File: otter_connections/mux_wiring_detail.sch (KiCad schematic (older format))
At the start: 21 parts

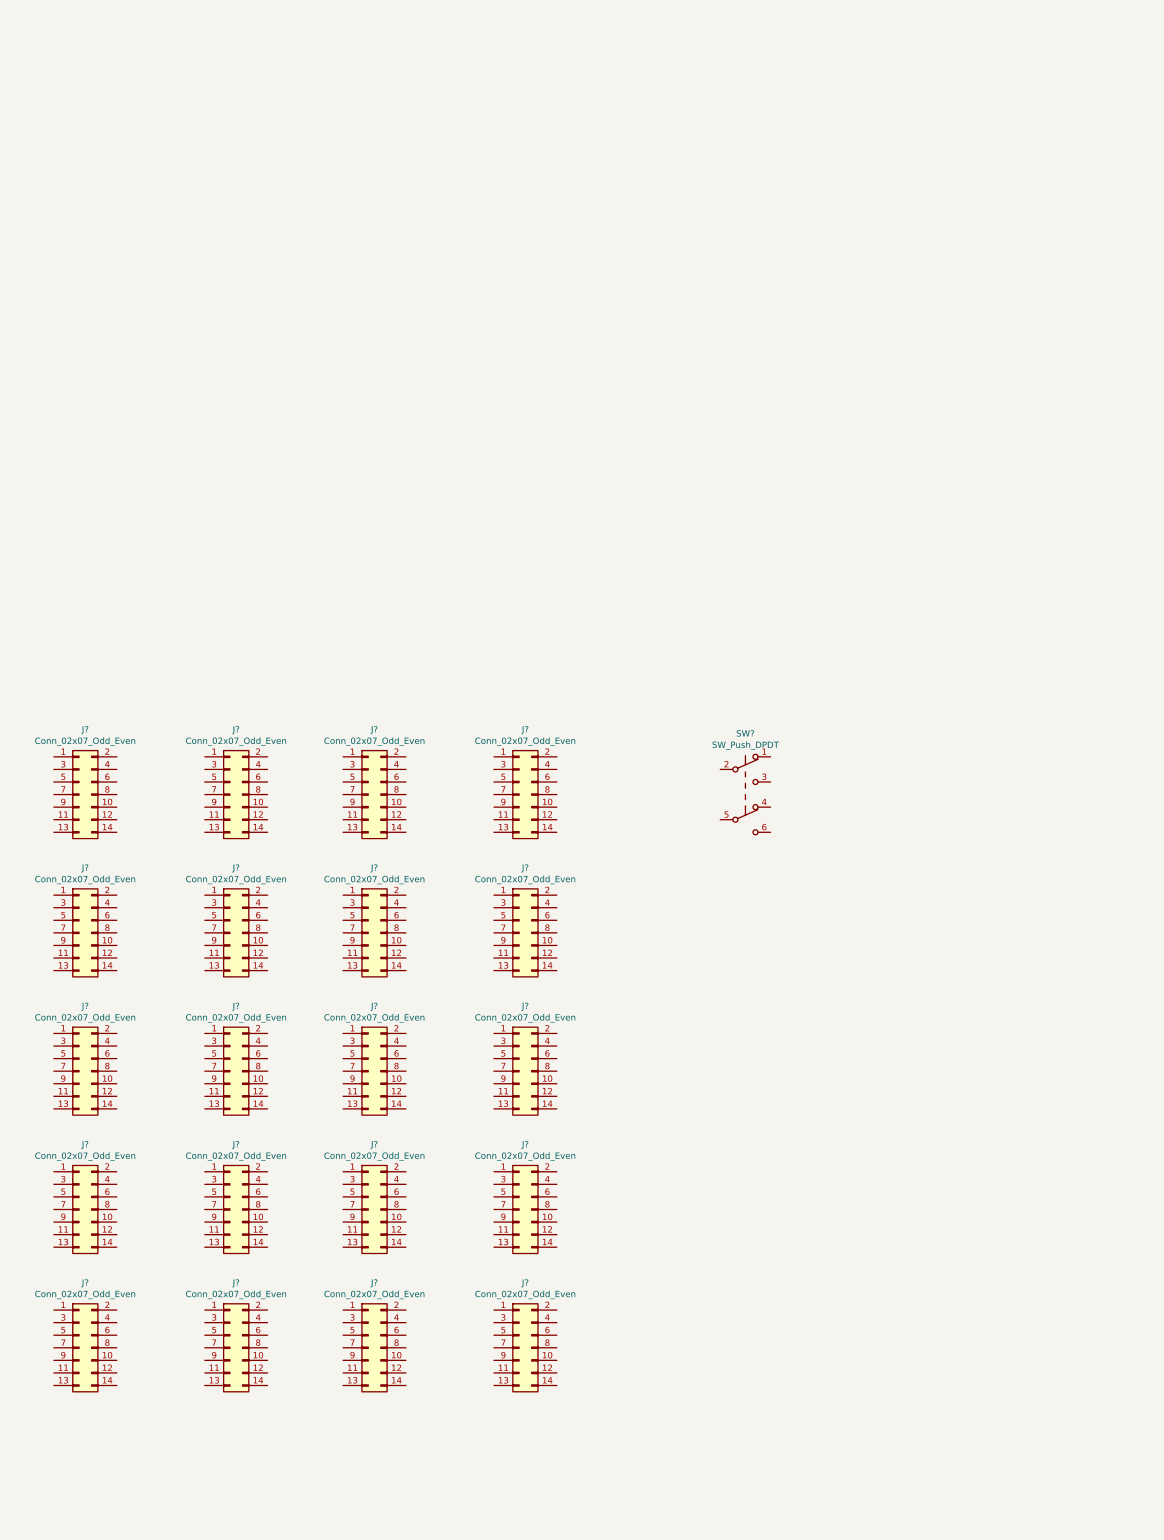
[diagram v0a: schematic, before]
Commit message: fix baseboard connector position
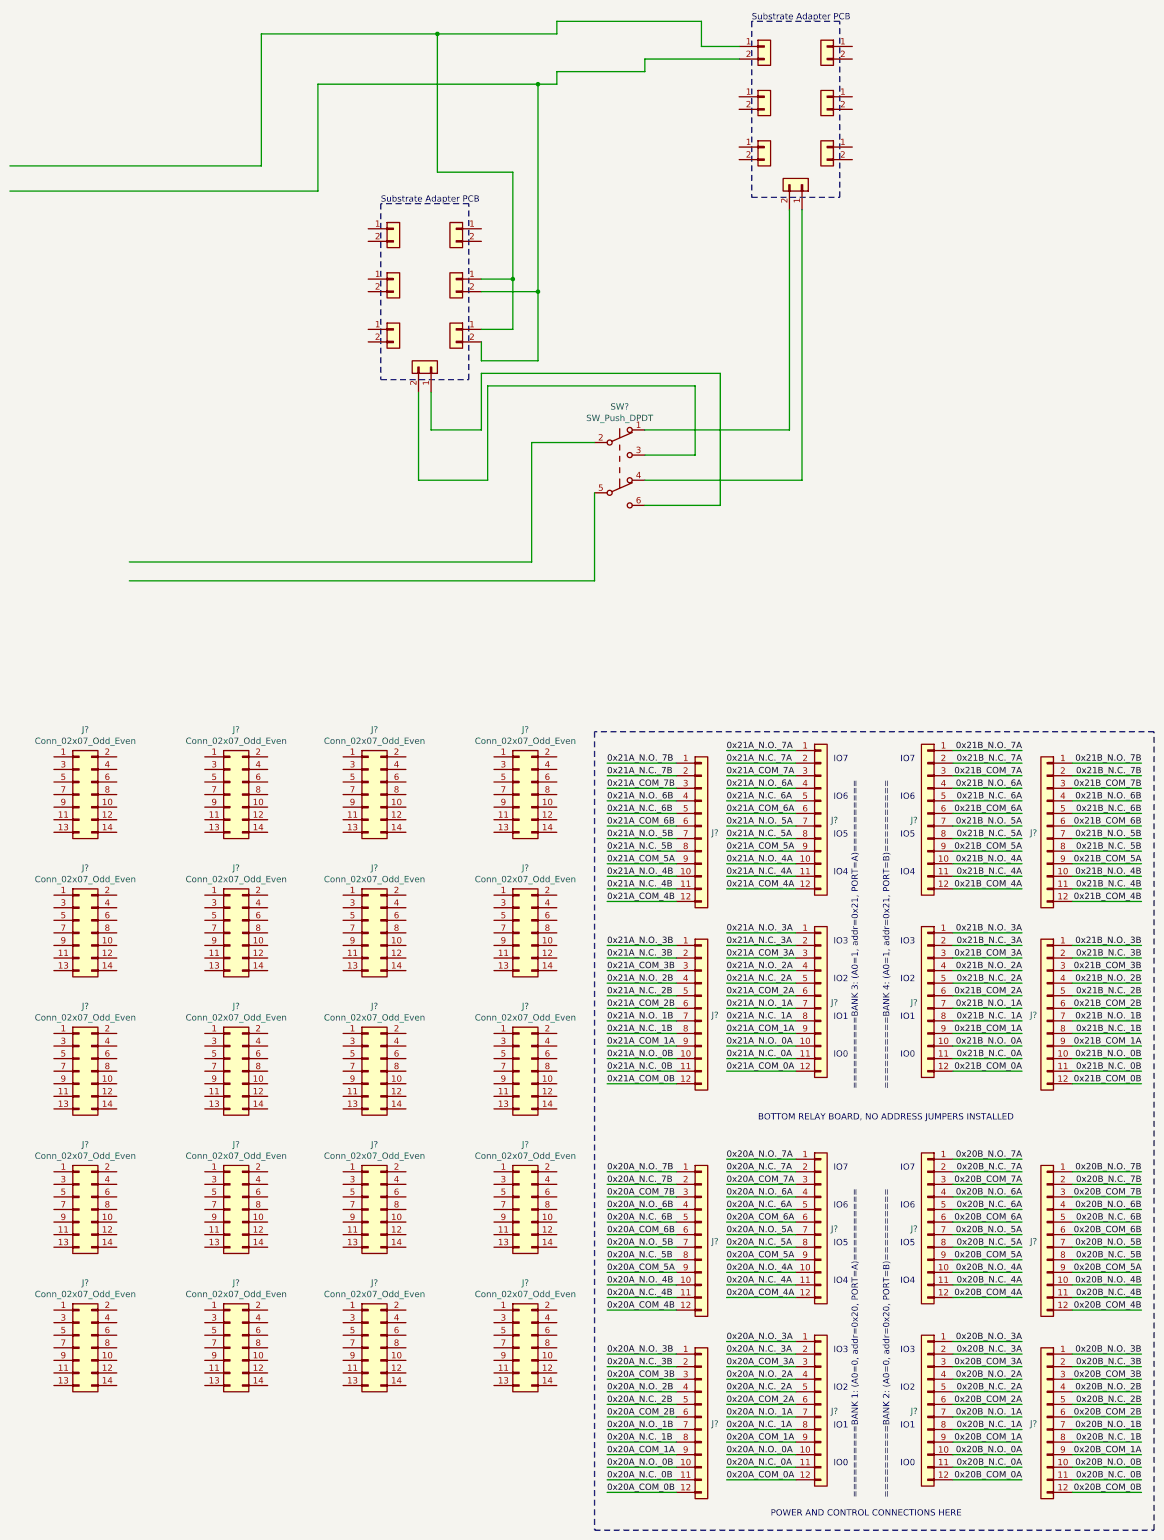
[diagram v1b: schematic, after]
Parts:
- removed SW?: SW_Push_DPDT, symbol Switch:SW_Push_DPDT
- added J? (x16): Conn_01x12, symbol Connector_Generic:Conn_01x12
- added J? (x14): Conn_01x02, symbol Connector_Generic:Conn_01x02
- added SW?: SW_Push_DPDT, symbol Switch:SW_Push_DPDT
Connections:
- new net: J?.1 (Pin_1), J?.1 (Pin_1), J?.1 (Pin_1)
- new net: J?.2 (Pin_2), J?.2 (Pin_2), J?.2 (Pin_2)
- new net: J?.1 (Pin_1), SW?.6 (C)
- new net: J?.2 (Pin_2), SW?.3 (C)
- new net: J?.1 (Pin_1), SW?.4 (A)
- new net: J?.2 (Pin_2), SW?.1 (A)
- new net 0x20A_COM_0A: J?.12 (Pin_12)
- new net 0x20A_COM_0B: J?.12 (Pin_12)
- new net 0x20A_COM_1A: J?.9 (Pin_9), J?.9 (Pin_9)
- new net 0x20A_COM_2A: J?.6 (Pin_6)
- new net 0x20A_COM_2B: J?.6 (Pin_6)
- new net 0x20A_COM_3A: J?.3 (Pin_3)
- new net 0x20A_COM_3B: J?.3 (Pin_3)
- new net 0x20A_COM_4A: J?.12 (Pin_12)
- new net 0x20A_COM_4B: J?.12 (Pin_12)
- new net 0x20A_COM_5A: J?.9 (Pin_9), J?.9 (Pin_9)
- new net 0x20A_COM_6A: J?.6 (Pin_6)
- new net 0x20A_COM_6B: J?.6 (Pin_6)
- new net 0x20A_COM_7A: J?.3 (Pin_3)
- new net 0x20A_COM_7B: J?.3 (Pin_3)
- new net 0x20A_N.C._0A: J?.11 (Pin_11)
- new net 0x20A_N.C._0B: J?.11 (Pin_11)
- new net 0x20A_N.C._1A: J?.8 (Pin_8)
- new net 0x20A_N.C._1B: J?.8 (Pin_8)
- new net 0x20A_N.C._2A: J?.5 (Pin_5)
- new net 0x20A_N.C._2B: J?.5 (Pin_5)
- new net 0x20A_N.C._3A: J?.2 (Pin_2)
- new net 0x20A_N.C._3B: J?.2 (Pin_2)
- new net 0x20A_N.C._4A: J?.11 (Pin_11)
- new net 0x20A_N.C._4B: J?.11 (Pin_11)
- new net 0x20A_N.C._5A: J?.8 (Pin_8)
- new net 0x20A_N.C._5B: J?.8 (Pin_8)
- new net 0x20A_N.C._6A: J?.5 (Pin_5)
- new net 0x20A_N.C._6B: J?.5 (Pin_5)
- new net 0x20A_N.C._7A: J?.2 (Pin_2)
- new net 0x20A_N.C._7B: J?.2 (Pin_2)
- new net 0x20A_N.O._0A: J?.10 (Pin_10)
- new net 0x20A_N.O._0B: J?.10 (Pin_10)
- new net 0x20A_N.O._1A: J?.7 (Pin_7)
- new net 0x20A_N.O._1B: J?.7 (Pin_7)
- new net 0x20A_N.O._2A: J?.4 (Pin_4)
- new net 0x20A_N.O._2B: J?.4 (Pin_4)
- new net 0x20A_N.O._3A: J?.1 (Pin_1)
- new net 0x20A_N.O._3B: J?.1 (Pin_1)
- new net 0x20A_N.O._4A: J?.10 (Pin_10)
- new net 0x20A_N.O._4B: J?.10 (Pin_10)
- new net 0x20A_N.O._5A: J?.7 (Pin_7)
- new net 0x20A_N.O._5B: J?.7 (Pin_7)
- new net 0x20A_N.O._6A: J?.4 (Pin_4)
- new net 0x20A_N.O._6B: J?.4 (Pin_4)
- new net 0x20A_N.O._7A: J?.1 (Pin_1)
- new net 0x20A_N.O._7B: J?.1 (Pin_1)
- new net 0x20B_COM_0A: J?.12 (Pin_12)
- new net 0x20B_COM_0B: J?.12 (Pin_12)
- new net 0x20B_COM_1A: J?.9 (Pin_9), J?.9 (Pin_9)
- new net 0x20B_COM_2A: J?.6 (Pin_6)
- new net 0x20B_COM_2B: J?.6 (Pin_6)
- new net 0x20B_COM_3A: J?.3 (Pin_3)
- new net 0x20B_COM_3B: J?.3 (Pin_3)
- new net 0x20B_COM_4A: J?.12 (Pin_12)
- new net 0x20B_COM_4B: J?.12 (Pin_12)
- new net 0x20B_COM_5A: J?.9 (Pin_9), J?.9 (Pin_9)
- new net 0x20B_COM_6A: J?.6 (Pin_6)
- new net 0x20B_COM_6B: J?.6 (Pin_6)
- new net 0x20B_COM_7A: J?.3 (Pin_3)
- new net 0x20B_COM_7B: J?.3 (Pin_3)
- new net 0x20B_N.C._0A: J?.11 (Pin_11)
- new net 0x20B_N.C._0B: J?.11 (Pin_11)
- new net 0x20B_N.C._1A: J?.8 (Pin_8)
- new net 0x20B_N.C._1B: J?.8 (Pin_8)
- new net 0x20B_N.C._2A: J?.5 (Pin_5)
- new net 0x20B_N.C._2B: J?.5 (Pin_5)
- new net 0x20B_N.C._3A: J?.2 (Pin_2)
- new net 0x20B_N.C._3B: J?.2 (Pin_2)
- new net 0x20B_N.C._4A: J?.11 (Pin_11)
- new net 0x20B_N.C._4B: J?.11 (Pin_11)
- new net 0x20B_N.C._5A: J?.8 (Pin_8)
- new net 0x20B_N.C._5B: J?.8 (Pin_8)
- new net 0x20B_N.C._6A: J?.5 (Pin_5)
- new net 0x20B_N.C._6B: J?.5 (Pin_5)
- new net 0x20B_N.C._7A: J?.2 (Pin_2)
- new net 0x20B_N.C._7B: J?.2 (Pin_2)
- new net 0x20B_N.O._0A: J?.10 (Pin_10)
- new net 0x20B_N.O._0B: J?.10 (Pin_10)
- new net 0x20B_N.O._1A: J?.7 (Pin_7)
- new net 0x20B_N.O._1B: J?.7 (Pin_7)
- new net 0x20B_N.O._2A: J?.4 (Pin_4)
- new net 0x20B_N.O._2B: J?.4 (Pin_4)
- new net 0x20B_N.O._3A: J?.1 (Pin_1)
- new net 0x20B_N.O._3B: J?.1 (Pin_1)
- new net 0x20B_N.O._4A: J?.10 (Pin_10)
- new net 0x20B_N.O._4B: J?.10 (Pin_10)
- new net 0x20B_N.O._5A: J?.7 (Pin_7)
- new net 0x20B_N.O._5B: J?.7 (Pin_7)
- new net 0x20B_N.O._6A: J?.4 (Pin_4)
- new net 0x20B_N.O._6B: J?.4 (Pin_4)
- new net 0x20B_N.O._7A: J?.1 (Pin_1)
- new net 0x20B_N.O._7B: J?.1 (Pin_1)
- new net 0x21A_COM_0A: J?.12 (Pin_12)
- new net 0x21A_COM_0B: J?.12 (Pin_12)
- new net 0x21A_COM_1A: J?.9 (Pin_9), J?.9 (Pin_9)
- new net 0x21A_COM_2A: J?.6 (Pin_6)
- new net 0x21A_COM_2B: J?.6 (Pin_6)
- new net 0x21A_COM_3A: J?.3 (Pin_3)
- new net 0x21A_COM_3B: J?.3 (Pin_3)
- new net 0x21A_COM_4A: J?.12 (Pin_12)
- new net 0x21A_COM_4B: J?.12 (Pin_12)
- new net 0x21A_COM_5A: J?.9 (Pin_9), J?.9 (Pin_9)
- new net 0x21A_COM_6A: J?.6 (Pin_6)
- new net 0x21A_COM_6B: J?.6 (Pin_6)
- new net 0x21A_COM_7A: J?.3 (Pin_3)
- new net 0x21A_COM_7B: J?.3 (Pin_3)
- new net 0x21A_N.C._0A: J?.11 (Pin_11)
- new net 0x21A_N.C._0B: J?.11 (Pin_11)
- new net 0x21A_N.C._1A: J?.8 (Pin_8)
- new net 0x21A_N.C._1B: J?.8 (Pin_8)
- new net 0x21A_N.C._2A: J?.5 (Pin_5)
- new net 0x21A_N.C._2B: J?.5 (Pin_5)
- new net 0x21A_N.C._3A: J?.2 (Pin_2)
- new net 0x21A_N.C._3B: J?.2 (Pin_2)
- new net 0x21A_N.C._4A: J?.11 (Pin_11)
- new net 0x21A_N.C._4B: J?.11 (Pin_11)
- new net 0x21A_N.C._5A: J?.8 (Pin_8)
- new net 0x21A_N.C._5B: J?.8 (Pin_8)
- new net 0x21A_N.C._6A: J?.5 (Pin_5)
- new net 0x21A_N.C._6B: J?.5 (Pin_5)
- new net 0x21A_N.C._7A: J?.2 (Pin_2)
- new net 0x21A_N.C._7B: J?.2 (Pin_2)
- new net 0x21A_N.O._0A: J?.10 (Pin_10)
- new net 0x21A_N.O._0B: J?.10 (Pin_10)
- new net 0x21A_N.O._1A: J?.7 (Pin_7)
- new net 0x21A_N.O._1B: J?.7 (Pin_7)
- new net 0x21A_N.O._2A: J?.4 (Pin_4)
- new net 0x21A_N.O._2B: J?.4 (Pin_4)
- new net 0x21A_N.O._3A: J?.1 (Pin_1)
- new net 0x21A_N.O._3B: J?.1 (Pin_1)
- new net 0x21A_N.O._4A: J?.10 (Pin_10)
- new net 0x21A_N.O._4B: J?.10 (Pin_10)
- new net 0x21A_N.O._5A: J?.7 (Pin_7)
- new net 0x21A_N.O._5B: J?.7 (Pin_7)
- new net 0x21A_N.O._6A: J?.4 (Pin_4)
- new net 0x21A_N.O._6B: J?.4 (Pin_4)
- new net 0x21A_N.O._7A: J?.1 (Pin_1)
- new net 0x21A_N.O._7B: J?.1 (Pin_1)
- new net 0x21B_COM_0A: J?.12 (Pin_12)
- new net 0x21B_COM_0B: J?.12 (Pin_12)
- new net 0x21B_COM_1A: J?.9 (Pin_9), J?.9 (Pin_9)
- new net 0x21B_COM_2A: J?.6 (Pin_6)
- new net 0x21B_COM_2B: J?.6 (Pin_6)
- new net 0x21B_COM_3A: J?.3 (Pin_3)
- new net 0x21B_COM_3B: J?.3 (Pin_3)
- new net 0x21B_COM_4A: J?.12 (Pin_12)
- new net 0x21B_COM_4B: J?.12 (Pin_12)
- new net 0x21B_COM_5A: J?.9 (Pin_9), J?.9 (Pin_9)
- new net 0x21B_COM_6A: J?.6 (Pin_6)
- new net 0x21B_COM_6B: J?.6 (Pin_6)
- new net 0x21B_COM_7A: J?.3 (Pin_3)
- new net 0x21B_COM_7B: J?.3 (Pin_3)
- new net 0x21B_N.C._0A: J?.11 (Pin_11)
- new net 0x21B_N.C._0B: J?.11 (Pin_11)
- new net 0x21B_N.C._1A: J?.8 (Pin_8)
- new net 0x21B_N.C._1B: J?.8 (Pin_8)
- new net 0x21B_N.C._2A: J?.5 (Pin_5)
- new net 0x21B_N.C._2B: J?.5 (Pin_5)
- new net 0x21B_N.C._3A: J?.2 (Pin_2)
- new net 0x21B_N.C._3B: J?.2 (Pin_2)
- new net 0x21B_N.C._4A: J?.11 (Pin_11)
- new net 0x21B_N.C._4B: J?.11 (Pin_11)
- new net 0x21B_N.C._5A: J?.8 (Pin_8)
- new net 0x21B_N.C._5B: J?.8 (Pin_8)
- new net 0x21B_N.C._6A: J?.5 (Pin_5)
- new net 0x21B_N.C._6B: J?.5 (Pin_5)
- new net 0x21B_N.C._7A: J?.2 (Pin_2)
- new net 0x21B_N.C._7B: J?.2 (Pin_2)
- new net 0x21B_N.O._0A: J?.10 (Pin_10)
- new net 0x21B_N.O._0B: J?.10 (Pin_10)
- new net 0x21B_N.O._1A: J?.7 (Pin_7)
- new net 0x21B_N.O._1B: J?.7 (Pin_7)
- new net 0x21B_N.O._2A: J?.4 (Pin_4)
- new net 0x21B_N.O._2B: J?.4 (Pin_4)
- new net 0x21B_N.O._3A: J?.1 (Pin_1)
- new net 0x21B_N.O._3B: J?.1 (Pin_1)
- new net 0x21B_N.O._4A: J?.10 (Pin_10)
- new net 0x21B_N.O._4B: J?.10 (Pin_10)
- new net 0x21B_N.O._5A: J?.7 (Pin_7)
- new net 0x21B_N.O._5B: J?.7 (Pin_7)
- new net 0x21B_N.O._6A: J?.4 (Pin_4)
- new net 0x21B_N.O._6B: J?.4 (Pin_4)
- new net 0x21B_N.O._7A: J?.1 (Pin_1)
- new net 0x21B_N.O._7B: J?.1 (Pin_1)
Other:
- note added: "==========BANK 1: (A0=0, addr=0x20, PORT=A)=========="
- note added: "==========BANK 2: (A0=0, addr=0x20, PORT=B)=========="
- note added: "==========BANK 3: (A0=1, addr=0x21, PORT=A)=========="
- note added: "==========BANK 4: (A0=1, addr=0x21, PORT=B)=========="
- note added: "BOTTOM RELAY BOARD, NO ADDRESS JUMPERS INSTALLED"
- note added: "IO0"
- note added: "IO1"
- note added: "IO2"
- note added: "IO3"
- note added: "IO4"
- note added: "IO5"
- note added: "IO6"
- note added: "IO7"
- note added: "POWER AND CONTROL CONNECTIONS HERE"
- note added: "Substrate Adapter PCB"
